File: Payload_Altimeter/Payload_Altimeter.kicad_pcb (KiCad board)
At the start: 2 copper layers, 80 x 93.3 mm, 5 parts, among them J1 L717SDC37P1ACH4F, J2 Conn_01x09, U1 Arduino_Pro_Mini, U7 MS5607-02BA

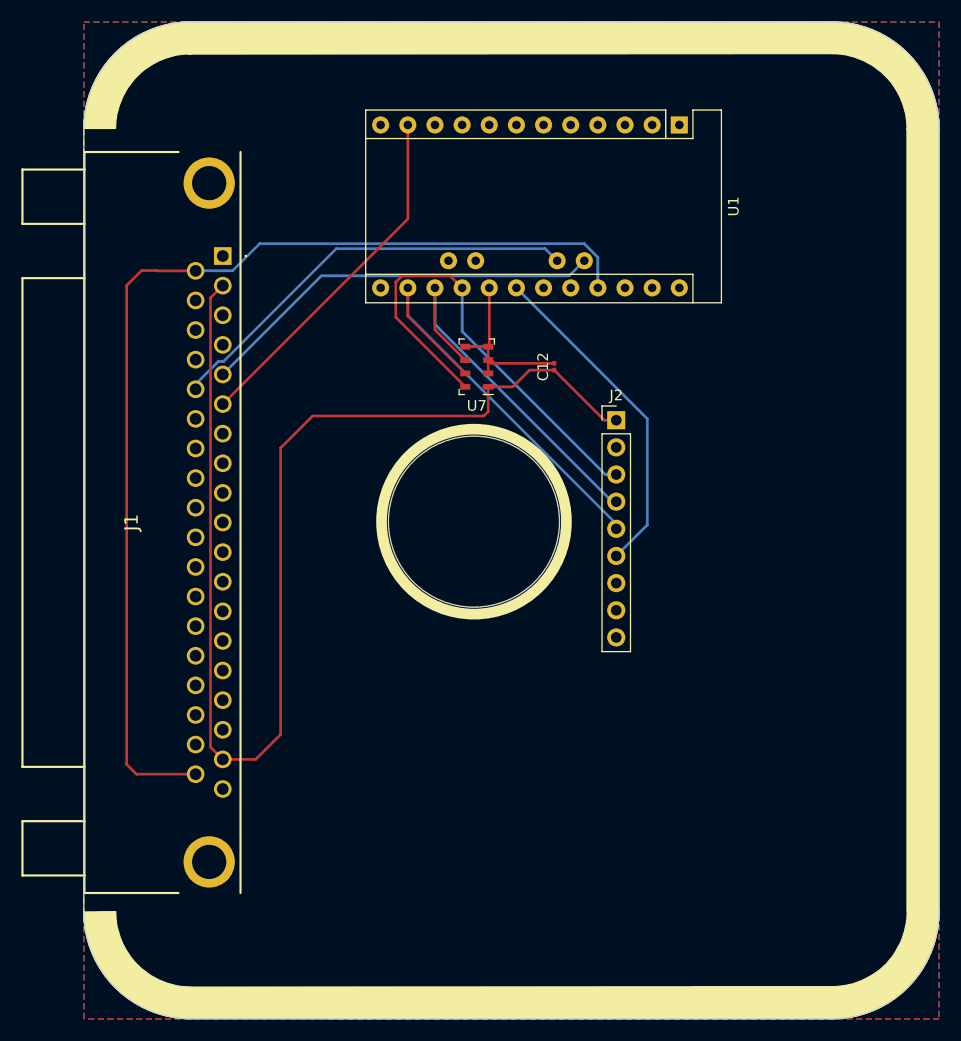
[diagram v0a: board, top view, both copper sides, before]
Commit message: Adjusted copper pours
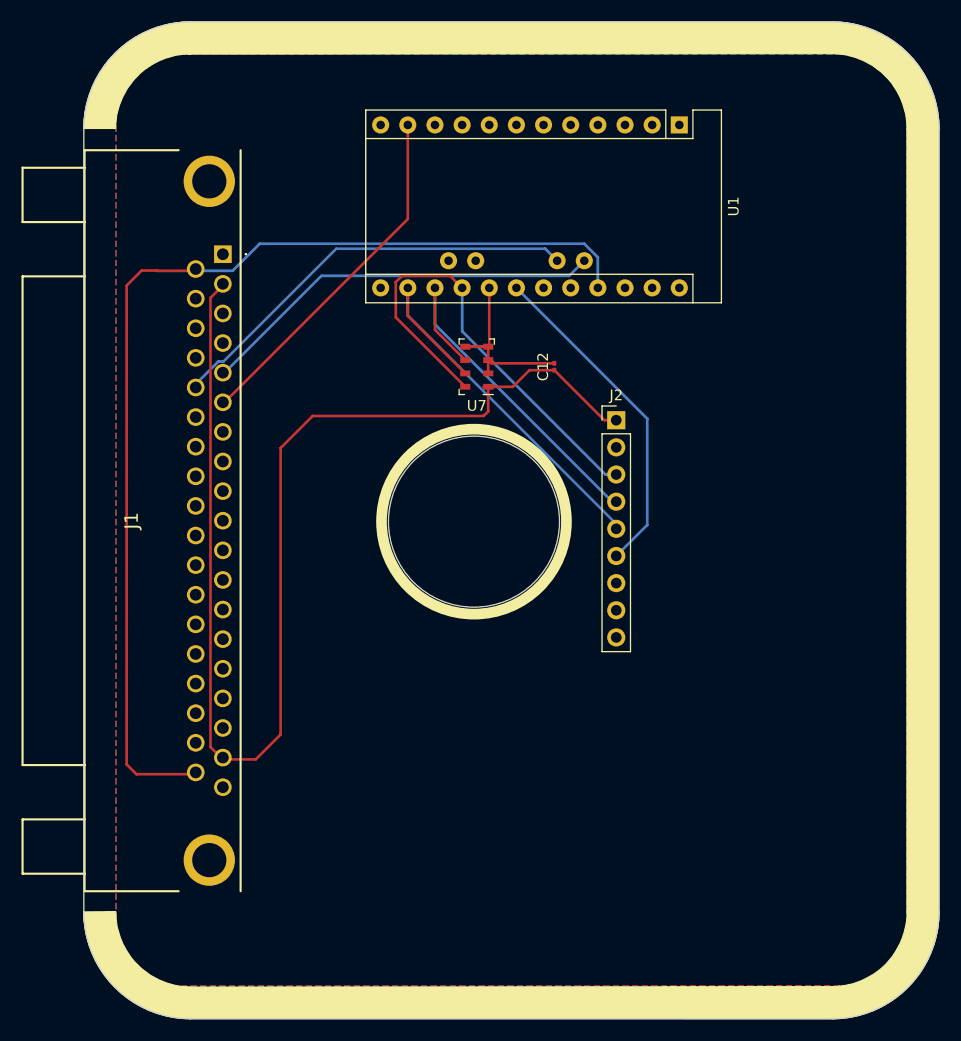
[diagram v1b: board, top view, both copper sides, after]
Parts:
- moved J1 0.17 mm to (93.0, 73.5)
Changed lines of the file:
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@@
   )
   (footprint "RDT_Custom_Footprints:L717SDC37P1ACH4F" (layer "F.Cu")
-    (at 92.98989 73.63989 -90)
+    (at 93 73.4725 -90)
     (descr "L717SDC37P1ACH4F-1")
     (tags "Connector")
@@
   (segment (start 117.92 82.03) (end 117.92 76.62) (width 0.25) (layer "F.Cu") (net 60))
   (zone (net 2) (net_name "GND") (layer "F.Cu") (hatch edge 0.508)
-    (connect_pads (clearance 0.508))
-    (min_thickness 0.254) (filled_areas_thickness no)
-    (fill yes (thermal_gap 0.508) (thermal_bridge_width 0.508))
+    (connect_pads (clearance 0.5))
+    (min_thickness 0.2) (filled_areas_thickness no)
+    (fill yes (thermal_gap 0.508) (thermal_bridge_width 0.508) (smoothing fillet) (radius 7))
     (polygon
       (pts
-        (xy 160 145)
-        (xy 80 145)
-        (xy 80 51.75)
-        (xy 160 51.75)
+        (xy 157 54.725)
+        (xy 157 141.9)
+        (xy 83 141.925)
+        (xy 83 54.725)
       )
     )
   )
   (zone (net 2) (net_name "GND") (layer "B.Cu") (hatch edge 0.508)
-    (connect_pads (clearance 0.508))
-    (min_thickness 0.254) (filled_areas_thickness no)
-    (fill yes (thermal_gap 0.508) (thermal_bridge_width 0.508))
+    (connect_pads (clearance 0.5))
+    (min_thickness 0.2) (filled_areas_thickness no)
+    (fill yes (thermal_gap 0.508) (thermal_bridge_width 0.508) (smoothing fillet) (radius 7))
     (polygon
       (pts
-        (xy 160 145)
-        (xy 80 145)
-        (xy 80 51.75)
-        (xy 160 51.75)
+        (xy 157 54.725)
+        (xy 157 141.9)
+        (xy 83 141.925)
+        (xy 83 54.725)
       )
     )
